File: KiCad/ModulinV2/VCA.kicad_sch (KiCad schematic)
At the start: 13 parts, among them IC28 TL072HIDR, IC29 AS3360D

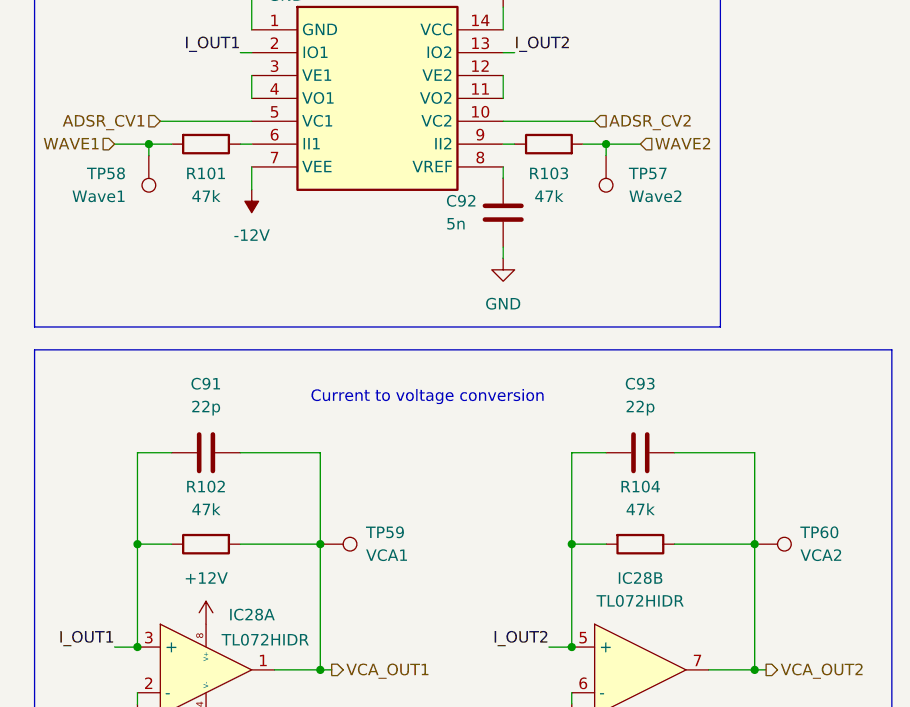
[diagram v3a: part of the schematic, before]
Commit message: Added footprints to all capacitors and potentiometers
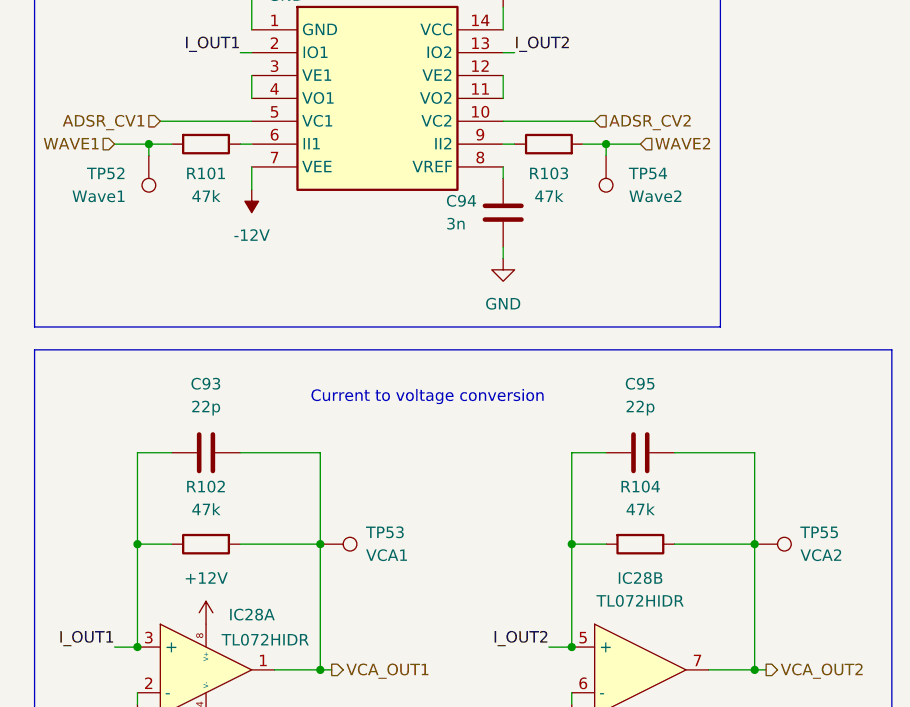
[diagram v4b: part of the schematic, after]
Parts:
- C93: renamed from C91; footprint (none) -> Capacitor_SMD:C_0603_1608Metric_Pad1.08x0.95mm_HandSolder
- C94: renamed from C92; value 5n -> 3n; footprint (none) -> Capacitor_SMD:C_0603_1608Metric_Pad1.08x0.95mm_HandSolder
- C95: renamed from C93; footprint (none) -> Capacitor_SMD:C_0603_1608Metric_Pad1.08x0.95mm_HandSolder
- renumbered TP58 to TP52, TP59 to TP53, TP57 to TP54, TP60 to TP55
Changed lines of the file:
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@@
 		(dnp no)
 		(fields_autoplaced yes)
-		(property "Reference" "#PWR0212"
+		(property "Reference" "#PWR0214"
 			(at 66.04 30.48 0)
 			(effects
@@
 			(project ""
 				(path "/c6b34a57-3941-4b56-8b80-1848c7f41082/a5a8abcc-50bb-4382-96d0-cbdb724bb6e9"
-					(reference "#PWR0212")
+					(reference "#PWR0214")
 					(unit 1)
 				)
@@
 		(dnp no)
 		(fields_autoplaced yes)
-		(property "Reference" "TP59"
+		(property "Reference" "TP53"
 			(at 50.8 85.0899 90)
 			(effects
@@
 			(project "ModulinV2"
 				(path "/c6b34a57-3941-4b56-8b80-1848c7f41082/a5a8abcc-50bb-4382-96d0-cbdb724bb6e9"
-					(reference "TP59")
+					(reference "TP53")
 					(unit 1)
 				)
@@
 		(dnp no)
 		(fields_autoplaced yes)
-		(property "Reference" "#PWR0208"
+		(property "Reference" "#PWR0210"
 			(at 33.02 99.06 0)
 			(effects
@@
 			(project "ModulinV2"
 				(path "/c6b34a57-3941-4b56-8b80-1848c7f41082/a5a8abcc-50bb-4382-96d0-cbdb724bb6e9"
-					(reference "#PWR0208")
+					(reference "#PWR0210")
 					(unit 1)
 				)
@@
 		(dnp no)
 		(fields_autoplaced yes)
-		(property "Reference" "#PWR0207"
+		(property "Reference" "#PWR0209"
 			(at 25.4 110.49 0)
 			(effects
@@
 			(project ""
 				(path "/c6b34a57-3941-4b56-8b80-1848c7f41082/a5a8abcc-50bb-4382-96d0-cbdb724bb6e9"
-					(reference "#PWR0207")
+					(reference "#PWR0209")
 					(unit 1)
 				)
@@
 		(dnp no)
 		(fields_autoplaced yes)
-		(property "Reference" "#PWR0213"
+		(property "Reference" "#PWR0215"
 			(at 66.04 60.96 0)
 			(effects
@@
 			(project ""
 				(path "/c6b34a57-3941-4b56-8b80-1848c7f41082/a5a8abcc-50bb-4382-96d0-cbdb724bb6e9"
-					(reference "#PWR0213")
+					(reference "#PWR0215")
 					(unit 1)
 				)
@@
 		(dnp no)
 		(fields_autoplaced yes)
-		(property "Reference" "#PWR0210"
+		(property "Reference" "#PWR0212"
 			(at 38.1 43.18 0)
 			(effects
@@
 			(project ""
 				(path "/c6b34a57-3941-4b56-8b80-1848c7f41082/a5a8abcc-50bb-4382-96d0-cbdb724bb6e9"
-					(reference "#PWR0210")
+					(reference "#PWR0212")
 					(unit 1)
 				)
@@
 		(on_board yes)
 		(dnp no)
-		(property "Reference" "TP58"
+		(property "Reference" "TP52"
 			(at 24.13 45.2119 0)
 			(effects
@@
 			(project "ModulinV2"
 				(path "/c6b34a57-3941-4b56-8b80-1848c7f41082/a5a8abcc-50bb-4382-96d0-cbdb724bb6e9"
-					(reference "TP58")
+					(reference "TP52")
 					(unit 1)
 				)
@@
 		(dnp no)
 		(fields_autoplaced yes)
-		(property "Reference" "#PWR0211"
+		(property "Reference" "#PWR0213"
 			(at 41.91 26.67 0)
 			(effects
@@
 			(project ""
 				(path "/c6b34a57-3941-4b56-8b80-1848c7f41082/a5a8abcc-50bb-4382-96d0-cbdb724bb6e9"
-					(reference "#PWR0211")
+					(reference "#PWR0213")
 					(unit 1)
 				)
@@
 		(dnp no)
 		(fields_autoplaced yes)
-		(property "Reference" "C91"
+		(property "Reference" "C93"
 			(at 33.02 68.58 90)
 			(effects
@@
 			)
 		)
-		(property "Footprint" ""
+		(property "Footprint" "Capacitor_SMD:C_0603_1608Metric_Pad1.08x0.95mm_HandSolder"
 			(at 29.21 75.2348 0)
 			(effects
@@
 			(project ""
 				(path "/c6b34a57-3941-4b56-8b80-1848c7f41082/a5a8abcc-50bb-4382-96d0-cbdb724bb6e9"
-					(reference "C91")
+					(reference "C93")
 					(unit 1)
 				)
@@
 		(dnp no)
 		(fields_autoplaced yes)
-		(property "Reference" "#PWR0209"
+		(property "Reference" "#PWR0211"
 			(at 33.02 101.6 0)
 			(effects
@@
 			(project "ModulinV2"
 				(path "/c6b34a57-3941-4b56-8b80-1848c7f41082/a5a8abcc-50bb-4382-96d0-cbdb724bb6e9"
-					(reference "#PWR0209")
+					(reference "#PWR0211")
 					(unit 1)
 				)
@@
 		(on_board yes)
 		(dnp no)
-		(property "Reference" "C92"
+		(property "Reference" "C94"
 			(at 59.69 48.26 0)
 			(effects
@@
 			)
 		)
-		(property "Value" "5n"
+		(property "Value" "3n"
 			(at 59.69 50.8 0)
 			(effects
@@
 			)
 		)
-		(property "Footprint" ""
+		(property "Footprint" "Capacitor_SMD:C_0603_1608Metric_Pad1.08x0.95mm_HandSolder"
 			(at 67.0052 53.34 0)
 			(effects
@@
 			(project ""
 				(path "/c6b34a57-3941-4b56-8b80-1848c7f41082/a5a8abcc-50bb-4382-96d0-cbdb724bb6e9"
-					(reference "C92")
+					(reference "C94")
 					(unit 1)
 				)
@@
 		(dnp no)
 		(fields_autoplaced yes)
-		(property "Reference" "#PWR0214"
+		(property "Reference" "#PWR0216"
 			(at 73.66 110.49 0)
 			(effects
@@
 			(project ""
 				(path "/c6b34a57-3941-4b56-8b80-1848c7f41082/a5a8abcc-50bb-4382-96d0-cbdb724bb6e9"
-					(reference "#PWR0214")
+					(reference "#PWR0216")
 					(unit 1)
 				)
@@
 		(dnp no)
 		(fields_autoplaced yes)
-		(property "Reference" "TP60"
+		(property "Reference" "TP55"
 			(at 99.06 85.0899 90)
 			(effects
@@
 			(project "ModulinV2"
 				(path "/c6b34a57-3941-4b56-8b80-1848c7f41082/a5a8abcc-50bb-4382-96d0-cbdb724bb6e9"
-					(reference "TP60")
+					(reference "TP55")
 					(unit 1)
 				)
@@
 		(dnp no)
 		(fields_autoplaced yes)
-		(property "Reference" "C93"
+		(property "Reference" "C95"
 			(at 81.28 68.58 90)
 			(effects
@@
 			)
 		)
-		(property "Footprint" ""
+		(property "Footprint" "Capacitor_SMD:C_0603_1608Metric_Pad1.08x0.95mm_HandSolder"
 			(at 85.09 75.2348 0)
 			(effects
@@
 			(project ""
 				(path "/c6b34a57-3941-4b56-8b80-1848c7f41082/a5a8abcc-50bb-4382-96d0-cbdb724bb6e9"
-					(reference "C93")
+					(reference "C95")
 					(unit 1)
 				)
@@
 		(dnp no)
 		(fields_autoplaced yes)
-		(property "Reference" "TP57"
+		(property "Reference" "TP54"
 			(at 80.01 45.2119 0)
 			(effects
@@
 			(project "ModulinV2"
 				(path "/c6b34a57-3941-4b56-8b80-1848c7f41082/a5a8abcc-50bb-4382-96d0-cbdb724bb6e9"
-					(reference "TP57")
-					(unit 1)
-				)
+					(reference "TP54")
+					(unit 1)
+				)

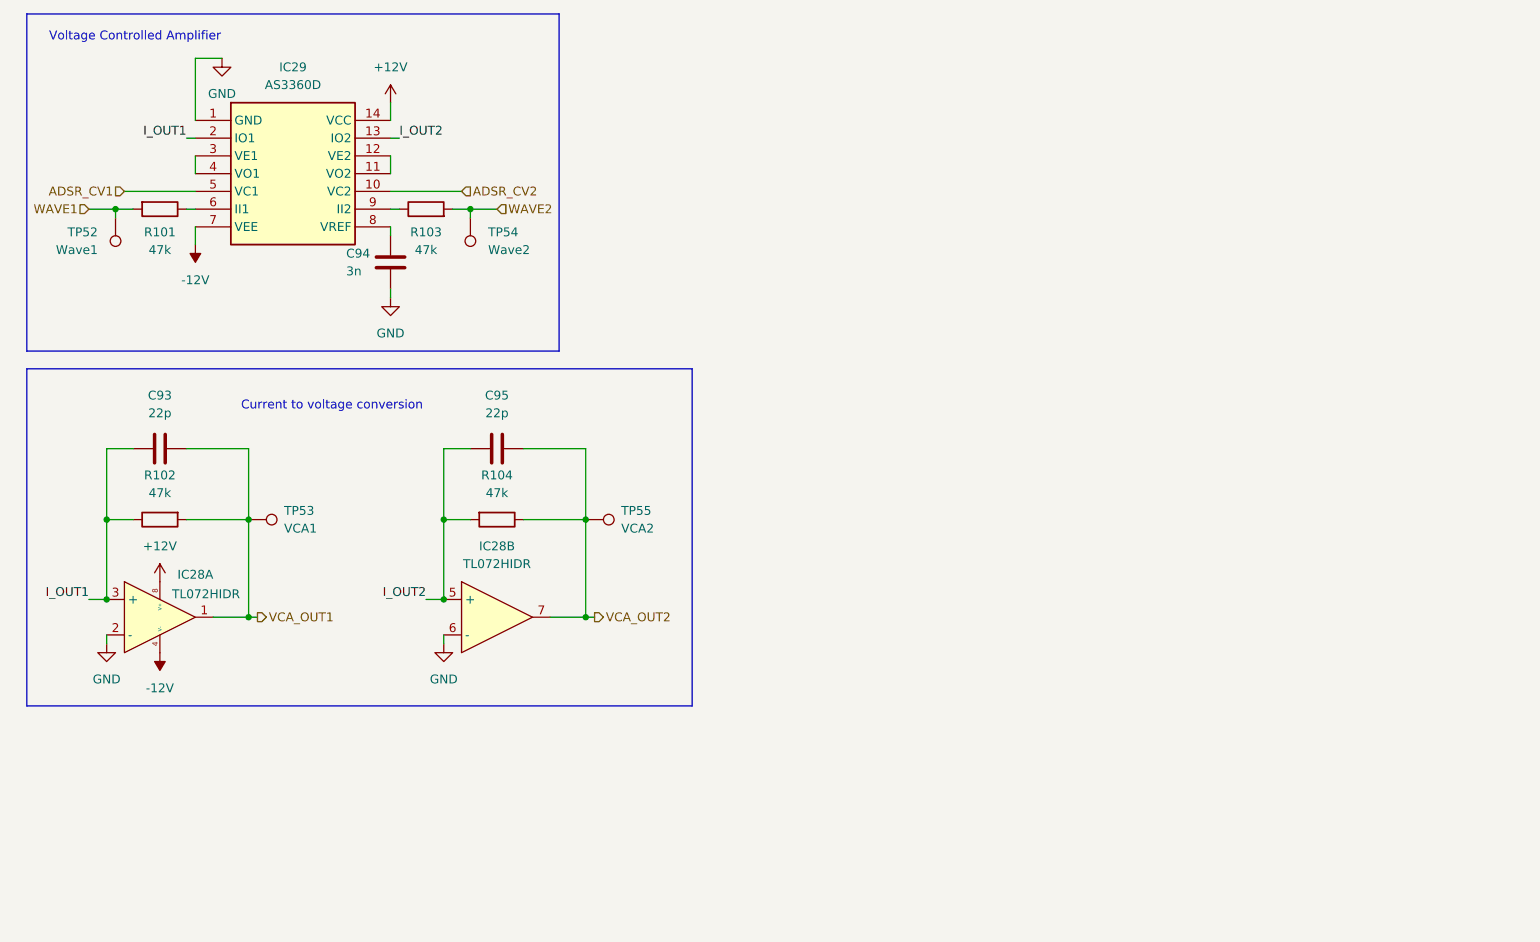
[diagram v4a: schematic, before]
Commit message: Finished Schematic, started on PCB
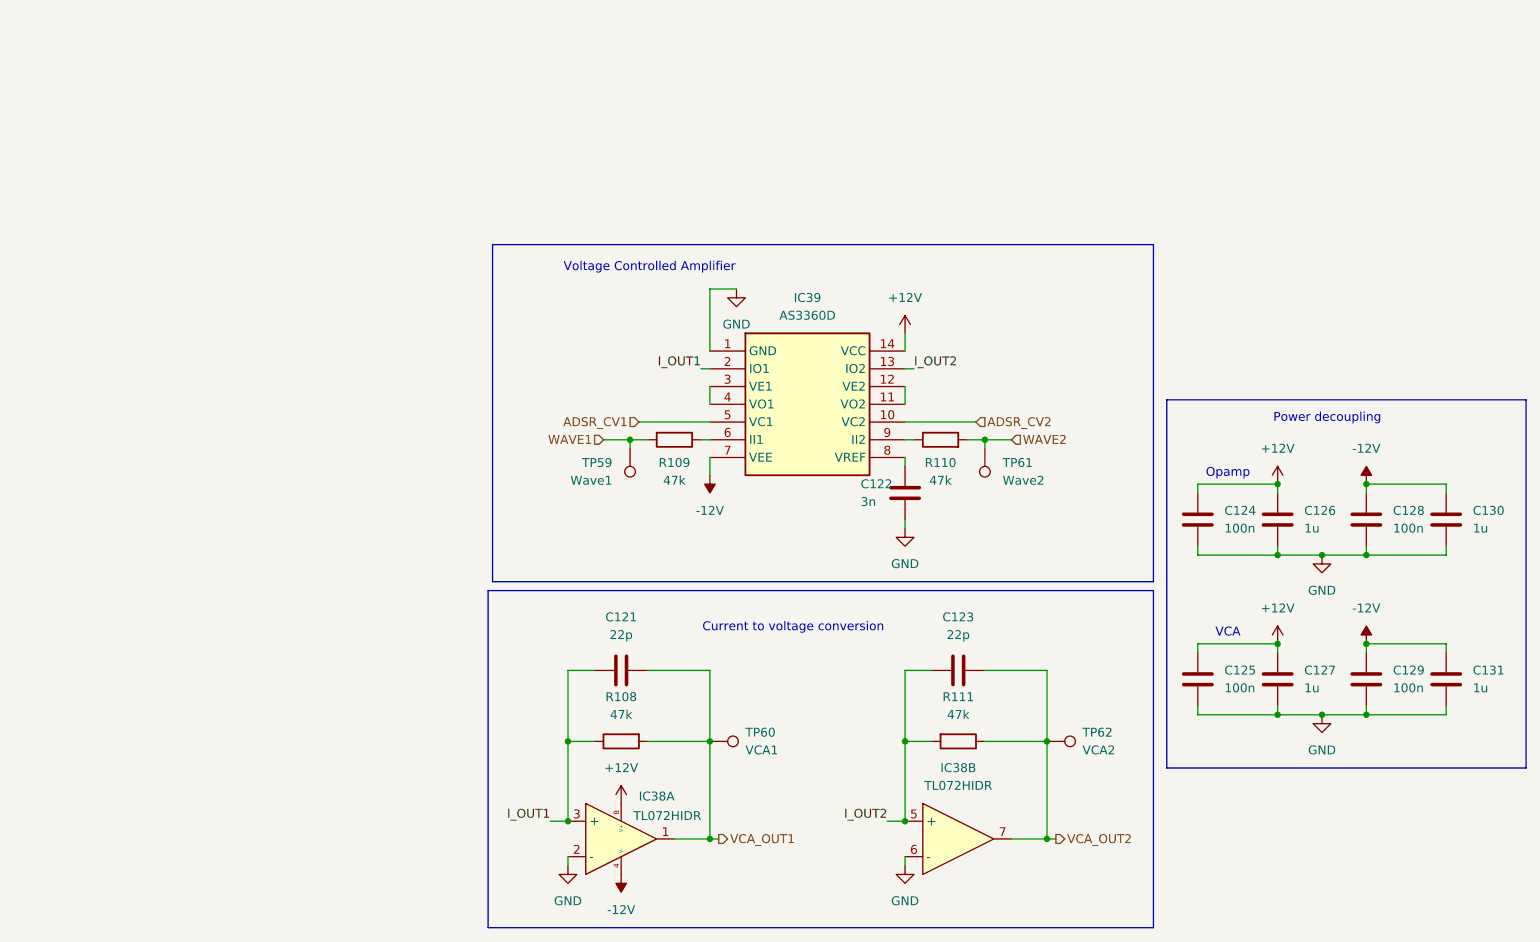
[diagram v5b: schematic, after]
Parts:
- added C124, C125, C128, C129: 100n, Capacitor_SMD:C_0603_1608Metric_Pad1.08x0.95mm_HandSolder, symbol Device:C
- added C126, C127, C130, C131: 1u, Capacitor_SMD:C_0603_1608Metric_Pad1.08x0.95mm_HandSolder, symbol Device:C
- IC39: renamed from IC29; footprint SamacSys_Parts:SOIC127P620X175-14N -> Package_SO:SOIC-14_3.9x8.7mm_P1.27mm
- R108: renamed from R102; footprint (none) -> Resistor_SMD:R_0805_2012Metric_Pad1.20x1.40mm_HandSolder
- R109: renamed from R101; footprint (none) -> Resistor_SMD:R_0805_2012Metric_Pad1.20x1.40mm_HandSolder
- R110: renamed from R103; footprint (none) -> Resistor_SMD:R_0805_2012Metric_Pad1.20x1.40mm_HandSolder
- R111: renamed from R104; footprint (none) -> Resistor_SMD:R_0805_2012Metric_Pad1.20x1.40mm_HandSolder
- renumbered C93 to C121, C94 to C122, C95 to C123, IC28 to IC38, TP52 to TP59, TP53 to TP60, TP54 to TP61, TP55 to TP62
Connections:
- net +12V: now also C124.2, C125.2, C126.2, C127.2
- net -12V: now also C128.2, C129.2, C130.2, C131.2
- net GND: now also C124.1, C125.1, C126.1, C127.1, C128.1, C129.1, C130.1, C131.1
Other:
- note added: "Opamp"
- note added: "Power decoupling"
- note added: "VCA"
- moved on the sheet: C121, C122, C123, IC38A, IC38B, IC39, R108, R109, R110, R111, TP59, TP60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
